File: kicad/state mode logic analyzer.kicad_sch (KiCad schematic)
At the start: 129 parts, among them J1 USB0, J2 Exp Out, J3 CLK 0-7, J4 8-15, J5 Exp In, J7 SWD0, J9 5V USB0, SW1 Reset 0, SW2 Boot 0, U1 RP2040, U10 74LVC245APW, U11 74LVC245APW, U3 74HC4520D, U4 LTC6994xS6-1, U5 MCP4725, U6 AD5241BRZ1M, U7 IS25LP128F-JBLE, U9 MCP1826S, Y1 ECS-120-18-33-JEM-TR

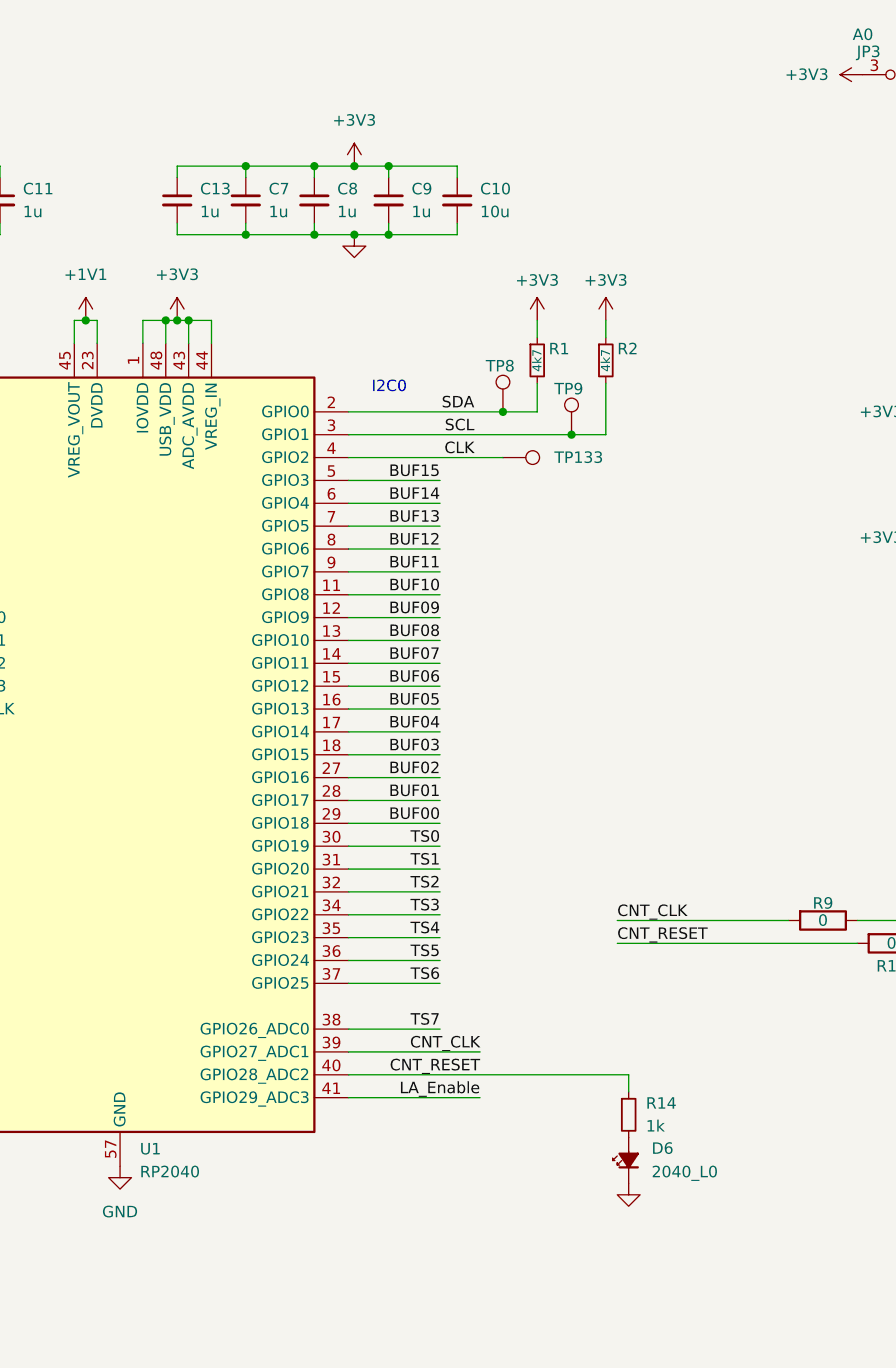
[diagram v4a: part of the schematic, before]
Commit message: passed drc and started silk clean up
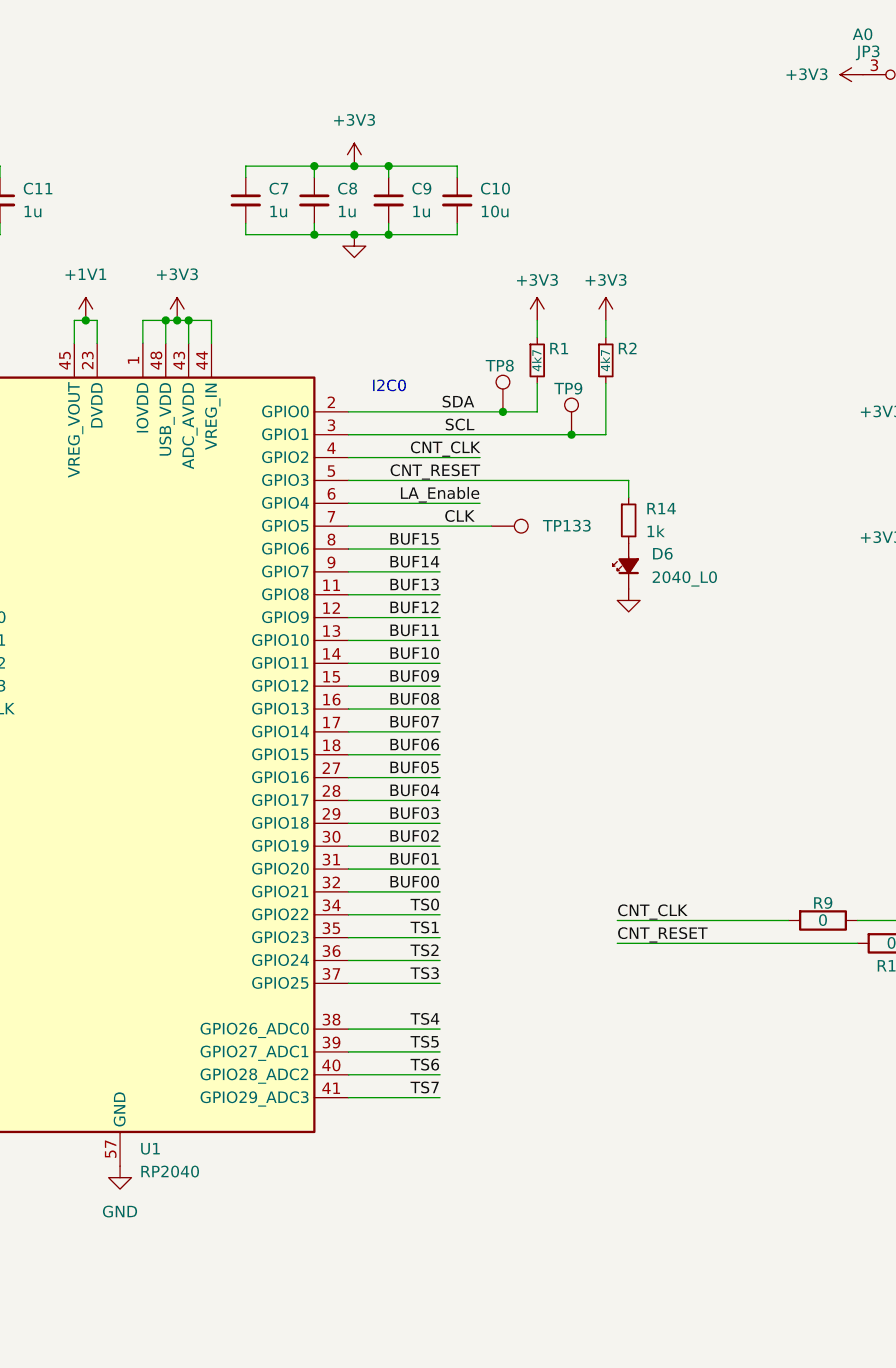
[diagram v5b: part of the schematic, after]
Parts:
- removed C13: 1u, Capacitor_SMD:C_0603_1608Metric_Pad1.08x0.95mm_HandSolder, symbol Device:C_Small
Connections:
- net BUF00: now also U1.32 (GPIO21); no longer U1.29 (GPIO18)
- net BUF01: now also U1.31 (GPIO20); no longer U1.28 (GPIO17)
- net BUF02: now also U1.30 (GPIO19); no longer U1.27 (GPIO16)
- net BUF03: now also U1.29 (GPIO18); no longer U1.18 (GPIO15)
- net BUF04: now also U1.28 (GPIO17); no longer U1.17 (GPIO14)
- net BUF05: now also U1.27 (GPIO16); no longer U1.16 (GPIO13)
- net BUF06: now also U1.18 (GPIO15); no longer U1.15 (GPIO12)
- net BUF07: now also U1.17 (GPIO14); no longer U1.14 (GPIO11)
- net BUF08: now also U1.16 (GPIO13); no longer U1.13 (GPIO10)
- net BUF09: now also U1.15 (GPIO12); no longer U1.12 (GPIO9)
- net BUF10: now also U1.14 (GPIO11); no longer U1.11 (GPIO8)
- net BUF11: now also U1.13 (GPIO10); no longer U1.9 (GPIO7)
- net BUF12: now also U1.12 (GPIO9); no longer U1.8 (GPIO6)
- net BUF13: now also U1.11 (GPIO8); no longer U1.7 (GPIO5)
- net BUF14: now also U1.9 (GPIO7); no longer U1.6 (GPIO4)
- net BUF15: now also U1.8 (GPIO6); no longer U1.5 (GPIO3)
- net CLK: now also U1.7 (GPIO5); no longer U1.4 (GPIO2)
- net CNT_CLK: now also U1.4 (GPIO2); no longer U1.39 (GPIO27_ADC1)
- net CNT_RESET: now also U1.5 (GPIO3); no longer U1.40 (GPIO28_ADC2)
- net LA_Enable: now also U1.6 (GPIO4); no longer U1.41 (GPIO29_ADC3)
- net TS0: now also U1.34 (GPIO22); no longer U1.30 (GPIO19)
- net TS1: now also U1.35 (GPIO23); no longer U1.31 (GPIO20)
- net TS2: now also U1.36 (GPIO24); no longer U1.32 (GPIO21)
- net TS3: now also U1.37 (GPIO25); no longer U1.34 (GPIO22)
- net TS4: now also U1.38 (GPIO26_ADC0); no longer U1.35 (GPIO23)
- net TS5: now also U1.39 (GPIO27_ADC1); no longer U1.36 (GPIO24)
- net TS6: now also U1.40 (GPIO28_ADC2); no longer U1.37 (GPIO25)
- net TS7: now also U1.41 (GPIO29_ADC3); no longer U1.38 (GPIO26_ADC0)
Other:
- moved on the sheet: D6, R14, TP133

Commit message: rev1 before verification
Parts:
- added TP15: TestPoint_Harwin, My Libraries:Harwin-S1751-46-Test-Point, symbol My Library:TestPoint_Harwin
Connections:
- net +3V3: now also TP15.1
- net AD0: now reaches JP1.1 (A), U6.8 (AD0)
- net AD1: now reaches JP2.1 (A), U6.9 (AD1)
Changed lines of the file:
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@@
     (effects (font (size 1.27 1.27)) (justify left bottom))
   )
+  (label "AD1" (at 405.13 120.65 0) (fields_autoplaced)
+    (effects (font (size 1.27 1.27)) (justify left bottom))
+  )
   (label "Run" (at 238.125 201.93 180) (fields_autoplaced)
     (effects (font (size 1.27 1.27)) (justify right bottom))
@@
     (effects (font (size 1.27 1.27)) (justify left bottom))
   )
+  (label "AD0" (at 405.13 118.11 0) (fields_autoplaced)
+    (effects (font (size 1.27 1.27)) (justify left bottom))
+  )
   (label "A8" (at 159.385 312.42 0) (fields_autoplaced)
     (effects (font (size 1.27 1.27)) (justify left bottom))
@@
     (pin "1")
     (pin "2")
-    (pin "4")
     (pin "3")
+    (pin "4")
     (instances
       (project "state mode logic analyzer"
@@
         )
       )
+    )
+  )
+  (symbol (lib_id "My Library:TestPoint_Harwin") (at 281.94 267.97 0) (unit 1)
+    (in_bom yes) (on_board yes) (dnp no)
+    (property "Reference" "TP15" (at 279.4 262.89 0)
+      (effects (font (size 1.27 1.27)) (justify left))
+    )
+    (property "Value" "TestPoint_Harwin" (at 281.94 262.89 0)
+      (effects (font (size 1.27 1.27)) hide)
+    )
+    (property "Footprint" "My Libraries:Harwin-S1751-46-Test-Point" (at 287.02 267.97 0)
+      (effects (font (size 1.27 1.27)) hide)
+    )
+    (property "Datasheet" "~" (at 287.02 267.97 0)
+      (effects (font (size 1.27 1.27)) hide)
+    )
+    (pin "1")
+    (instances
+      (project "state mode logic analyzer"
+        (path "/7975ca51-68cd-4bb7-8d39-236fa03ee415"
+          (reference "TP15") (unit 1)
+        )
+      )

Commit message: rneed to review again
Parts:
- removed C24: 1u, Capacitor_SMD:C_0603_1608Metric_Pad1.08x0.95mm_HandSolder, symbol Device:C_Small
- removed J3: CLK 0-7, Connector_PinHeader_2.54mm:PinHeader_2x10_P2.54mm_Vertical, symbol Connector_Generic:Conn_02x10_Odd_Even
- removed J4: 8-15, Connector_PinHeader_2.54mm:PinHeader_2x10_P2.54mm_Vertical, symbol Connector_Generic:Conn_02x10_Odd_Even
- added H1, H2, H3: MountingHole, MountingHole:MountingHole_2.7mm, symbol Mechanical:MountingHole
- added J6: Probe, Connector_PinHeader_2.54mm:PinHeader_2x12_P2.54mm_Vertical, symbol Connector_Generic:Conn_02x12_Odd_Even
- added J8: Probe Power, Connector_PinHeader_2.54mm:PinHeader_1x03_P2.54mm_Vertical, symbol Connector_Generic:Conn_01x03
- renumbered C25 to C24
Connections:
- net +3V3: now also J8.3 (Pin_3)
- net +5V: now also J8.1 (Pin_1)
- net GND: now also J6.1 (Pin_1), J6.13 (Pin_13), J6.14 (Pin_14), J6.19 (Pin_19), J6.20 (Pin_20), J6.7 (Pin_7), J6.8 (Pin_8), J8.2 (Pin_2)
- net IN00: now also J6.4 (Pin_4)
- net IN01: now also J6.3 (Pin_3)
- net IN02: now also J6.6 (Pin_6)
- net IN03: now also J6.5 (Pin_5)
- net IN04: now also J6.10 (Pin_10)
- net IN05: now also J6.9 (Pin_9)
- net IN06: now also J6.12 (Pin_12)
- net IN07: now also J6.11 (Pin_11)
- net IN08: now also J6.16 (Pin_16)
- net IN09: now also J6.15 (Pin_15)
- net IN10: now also J6.18 (Pin_18)
- net IN11: now also J6.17 (Pin_17)
- net IN12: now also J6.22 (Pin_22)
- net IN13: now also J6.21 (Pin_21)
- net IN14: now also J6.24 (Pin_24)
- net IN15: now also J6.23 (Pin_23)
- net IN_CLK: now also J6.2 (Pin_2)
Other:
- moved on the sheet: C23, C24, TP13

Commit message: Deocrated schematic
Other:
- note added: "Clock Delay"
- note added: "Extension Connectors"
- note added: "MCU (RP2040)"
- note added: "Power"
- note added: "Probe Inputs"
- note added: "Timestamp Counter"
- note added: "USB-C"
- moved on the sheet: C1, C10, C11, C12, C19, C2, C20, C21, C22, C23, C24, C3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
